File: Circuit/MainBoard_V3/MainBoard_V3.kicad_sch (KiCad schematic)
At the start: 0 parts

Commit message: 回路図と配置と配線が半分ほど終わり
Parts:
- added BZ1: Buzzer, Buzzer_Beeper:Buzzer_Murata_PKLCS1212E, symbol Device:Buzzer
- added C1, C12, C13, C14, C20, C21, C22, C23, C24, C26, C5: 0.1uf, Capacitor_SMD:C_0603_1608Metric, symbol Device:C
- added C10, C8: 100uf, Capacitor_THT:CP_Radial_D6.3mm_P2.50mm, symbol Device:C_Polarized
- added C11, C15, C17, C18, C19, C2, C27, C3, C4, C6, C7, C9: 10u, Capacitor_SMD:C_0805_2012Metric, symbol Device:C
- added C16: 4.7u, Capacitor_SMD:C_0805_2012Metric, symbol Device:C
- added C25: 2200pf, Capacitor_SMD:C_0603_1608Metric, symbol Device:C
- added D1, D2, D3, D7, D8: D_Schottky, Diode_SMD:D_SOD-323_HandSoldering, symbol Device:D_Schottky
- added D10, D11, D12, D13, D15, D16, D4, D5, D6, D9: LED, LED_SMD:LED_0603_1608Metric, symbol Device:LED
- added D14: CH213K, Package_TO_SOT_SMD:TSOT-23, symbol 0-MyLibrary:CH213K
- added F1, F2: Fuse, Fuse:Fuseholder_Clip-5x20mm_Keystone_3517_Inline_P23.11x6.76mm_D1.70mm_Horizontal, symbol Device:Fuse
- added H1, H2, H3, H4: MountingHole, MountingHole:MountingHole_3.2mm_M3_Pad_Via, symbol Mechanical:MountingHole
- added J1, J2, J3: Conn_01x02, Connector_JST:JST_PH_S2B-PH-K_1x02_P2.00mm_Horizontal, symbol Connector_Generic:Conn_01x02
- added J10, J11: Conn_01x03, Connector_JST:JST_PH_S3B-PH-K_1x03_P2.00mm_Horizontal, symbol Connector_Generic:Conn_01x03
- added J12, J13, J4: Conn_01x04, Connector_JST:JST_XH_S4B-XH-A-1_1x04_P2.50mm_Horizontal, symbol Connector_Generic:Conn_01x04
- added J14, J15: Conn_01x04, Connector_JST:JST_PH_S4B-PH-K_1x04_P2.00mm_Horizontal, symbol Connector_Generic:Conn_01x04
- added J5, J6, J7: Conn_01x02, Connector_Molex:Molex_SPOX_5268-02A_1x02_P2.50mm_Horizontal, symbol Connector_Generic:Conn_01x02
- added J8: Conn_01x07, Connector_JST:JST_PH_S7B-PH-K_1x07_P2.00mm_Horizontal, symbol Connector_Generic:Conn_01x07
- added J9: Raspberry_Pi_2_3, 0-MyLibrary:raspberreyPi, symbol Connector:Raspberry_Pi_2_3
- added MD1: OKL-T_6-W12N-C, 0-MyLibrary:MURATA_OKL-T-6-W12N-C_0, symbol OKL-T_6-W12N-C:OKL-T_6-W12N-C
- added NT1: NetTie_2, NetTie:NetTie-2_SMD_Pad0.5mm, symbol Device:NetTie_2
- added Q1, Q2: Q_PMOS_GDS, Package_TO_SOT_SMD:TO-252-2, symbol Device:Q_PMOS_GDS
- added Q10, Q3, Q5, Q6, Q7, Q8, Q9: BSS138, Package_TO_SOT_SMD:SOT-23, symbol Transistor_FET:BSS138
- added Q4: IRLML6402, Package_TO_SOT_SMD:SOT-23, symbol Transistor_FET:IRLML6402
- added R1, R13, R15, R17, R19, R2, R25, R26, R27, R30, R32, R34, R36, R37, R38, R4, R42, R5, R6, R7: 10k, Resistor_SMD:R_0603_1608Metric, symbol Device:R
- added R10, R12, R21, R29, R31, R33, R35, R41: 10, Resistor_SMD:R_0603_1608Metric, symbol Device:R
- added R11, R14, R16, R18, R20, R22, R23, R24, R28, R39, R40, R8: 1k, Resistor_SMD:R_0603_1608Metric, symbol Device:R
- added R9: 330, Resistor_SMD:R_0603_1608Metric, symbol Device:R
- added SW1, SW2, SW3: SW_Push, Button_Switch_SMD:SW_SPST_PTS810, symbol Switch:SW_Push
- added SW4, SW5: SW_Slide_DPDT, 0-MyLibrary:IS-2235, symbol Switch:SW_Slide_DPDT
- added TP1, TP2, TP3, TP4: TestPoint, TestPoint:TestPoint_THTPad_D4.0mm_Drill2.0mm, symbol Connector:TestPoint
- added TP5, TP6, TP7: TestPoint, TestPoint:TestPoint_THTPad_D1.0mm_Drill0.5mm, symbol Connector:TestPoint
- added U1: STM32F446RETx, Package_QFP:LQFP-64_10x10mm_P0.5mm, symbol MCU_ST_STM32F4:STM32F446RETx
- added U2: LM1117MP-3.3, Package_TO_SOT_SMD:SOT-223-3_TabPin2, symbol Regulator_Linear:LM1117MP-3.3
- added U3: MPU-6050, Package_DFN_QFN:QFN-24-1EP_4x4mm_P0.5mm_EP2.15x2.15mm, symbol Sensor_Motion:MPU-6050
- added Y1: CSTNE16M0V530000R0, Crystal:Resonator_SMD_Murata_CSTxExxV-3Pin_3.0x1.1mm, symbol CSTNE16M0V530000R0:CSTNE16M0V530000R0
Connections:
- new net: D4.2 (A), R11.1
- new net: Q4.1 (G), Q5.3 (D), R15.2
- new net: D10.2 (A), R23.1
- new net: Q8.1 (G), R33.2, R34.2
- new net: D12.2 (A), R25.1
- new net: Q2.1 (G), R5.2, SW5.1 (A), SW5.6 (C)
- new net: Q3.3 (D), SW5.2 (B), SW5.5 (B)
- new net: Q3.1 (G), R12.2, R13.2
- new net: D2.1 (K), F1.2, Q1.3 (S), R4.1
- new net: Q1.1 (G), R4.2, SW4.1 (A), SW4.6 (C)
- new net: Q7.1 (G), R31.2, R32.2
- new net: Q9.1 (G), R35.2, R36.2
- new net: Q5.1 (G), R21.1, R27.2
- new net: Q6.1 (G), R29.2, R30.2
- new net: C16.1, U1.30 (VCAP_1)
- new net: D13.2 (A), R26.1
- new net: D6.2 (A), R16.1
- new net: BZ1.2 (-), Q6.3 (D), R28.1
- new net: R10.1, R9.1
- new net: D15.2 (A), R39.1
- new net: D9.2 (A), R22.1
- new net: C18.1, D14.3 (VI), D8.2 (A), U2.2 (VO)
- new net: R8.1, R9.2
- new net: MD1.6 (TRIM), R8.2
- new net: D3.1 (K), F2.2, Q2.3 (S), R5.1
- new net: D5.2 (A), R14.1
- new net: D11.2 (A), R24.1
- new net: D16.2 (A), R40.1
- new net: C25.1, U3.20 (CPOUT)
- new net: R6.2, U1.60 (BOOT0)
- new net: Q10.1 (G), R41.2, R42.2
- new net: C26.1, U3.10 (REGOUT)
- new net: U1.5 (PH0), Y1.1
- new net: U1.6 (PH1), Y1.3
- new net: J9.1 (3V3), J9.17 (3V3)
- new net +3V3: C11.1, C14.2, C19.2, C20.2, C21.2, C22.2, C23.1, C24.2, D14.2 (VO), J10.2 (Pin_2), J11.2 (Pin_2), J12.2 (Pin_2), J13.2 (Pin_2), J8.2 (Pin_2), R1.2, R23.2, R37.1, R38.1, SW2.2, SW3.2, TP6.1, U1.1 (VBAT), U1.13 (VDDA), U1.19 (VDD), U1.32 (VDD), U1.48 (VDD), U1.64 (VDD), U3.13 (VDD), U3.8 (VLOGIC)
- new net +5V: C17.2, C27.1, C3.1, C4.1, C5.1, D1.2 (A), D7.1 (K), D8.1 (K), J14.4 (Pin_4), J15.4 (Pin_4), J9.2 (5V), J9.4 (5V), MD1.4 (VOUT), MD1.5 (SENSE), Q4.2 (S), R15.1, R24.2, TP5.1, U2.3 (VI)
- new net +BATT: F1.1, TP1.1
- new net +BATTP: F2.1, TP2.1
- new net ADC1: J10.3 (Pin_3), U1.24 (PC4)
- new net ADC2: J11.3 (Pin_3), U1.21 (PA5)
- new net ADC3: U1.20 (PA4)
- new net BRAKE_LED: J15.3 (Pin_3), Q8.3 (D)
- new net BRAKE_LED_SIG: R33.1, U1.26 (PB0)
- new net BTN1: R2.1, SW2.1, U1.3 (PC14)
- new net BTN2: R7.1, SW3.1, U1.2 (PC13)
- new net BUZZER: J9.12 (GPIO18/PWM0), R29.1, U1.55 (PB3)
- new net ECHO1: J12.3 (Pin_3), U1.50 (PA15)
- new net ECHO2: J13.3 (Pin_3), U1.41 (PA8)
- new net ECHO3: U1.40 (PC9)
- new net ECHO4: U1.36 (PB15)
- new net ECHO5: U1.34 (PB13)
- new net GND: C1.1, C11.2, C12.1, C14.1, C15.2, C16.2, C17.1, C18.2, C19.1, C2.1, C20.1, C21.1, C22.1, C23.2, C24.1, C25.2, C26.2, C27.2, C3.2, C4.2, C5.2, C6.2, C8.2, D10.1 (K), D11.1 (K), D12.1 (K), D14.1 (GND), D15.1 (K), D16.1 (K), D4.1 (K), D5.1 (K), D6.1 (K), D9.1 (K), J10.1 (Pin_1), J11.1 (Pin_1), J12.1 (Pin_1), J13.1 (Pin_1), J4.1 (Pin_1), J8.1 (Pin_1), J9.14 (GND), J9.20 (GND), J9.25 (GND), J9.30 (GND), J9.34 (GND), J9.39 (GND), J9.6 (GND), J9.9 (GND), MD1.1 (~{ON}/OFF_CONTROL), MD1.3 (1_GROUND), MD1.7 (2_GROUND), NT1.1, Q10.2 (S), Q5.2 (S), Q6.2 (S), Q7.2 (S), Q8.2 (S), Q9.2 (S), R10.2, R18.1, R2.2, R27.1, R30.1, R32.1, R34.1, R36.1, R42.1, R6.1, R7.2, SW1.1, SW4.2 (B), SW4.5 (B), TP3.1, TP7.1, U1.12 (VSSA), U1.18 (VSS), U1.31 (VSS), U1.47 (VSS), U1.63 (VSS), U2.1 (GND), U3.1 (CLKIN), U3.11 (FSYNC), U3.18 (GND), U3.9 (AD0), Y1.2
- new net GNDP: C10.2, C13.1, C7.1, C9.1, D13.1 (K), J5.1 (Pin_1), J6.1 (Pin_1), J7.1 (Pin_1), NT1.2, Q3.2 (S), R13.1, R20.1, TP4.1
- new net HEAD_LED: J14.3 (Pin_3), Q7.3 (D)
- new net HEAD_LED_SIG: R31.1, U1.27 (PB1)
- new net INT: U1.25 (PC5), U3.12 (INT)
- new net LIDAR_5V: C15.1, D7.2 (A), J4.2 (Pin_2), Q4.3 (D)
- new net LIDAR_5V_SIG: R21.2
- new net LIDAR_OUT: J4.3 (Pin_3), U1.44 (PA11)
- new net LW_LED: J14.2 (Pin_2), J15.2 (Pin_2), Q9.3 (D)
- new net LW_LED_SIG: R35.1, U1.23 (PA7)
- new net NRST: C1.2, J8.5 (Pin_5), R1.1, SW1.2, U1.7 (NRST)
- new net PC_RX: J8.7 (Pin_7), U1.42 (PA9)
- new net PC_TX: J8.6 (Pin_6), U1.43 (PA10)
- new net POWER_SIG: R12.1
- new net RAS_LED1: J9.35 (GPIO19/MISO1), R39.2
- new net RAS_LED2: J9.33 (PWM1/GPIO13), R40.2
- new net RAS_RX: J9.10 (GPIO15/RXD), U1.37 (PC6)
- new net RAS_TX: J9.8 (GPIO14/TXD), U1.38 (PC7)
- new net RW_LED: J14.1 (Pin_1), J15.1 (Pin_1), Q10.3 (D)
- new net RW_LED_SIG: R41.1, U1.22 (PA6)
- new net RX2: J1.2 (Pin_2), U1.17 (PA3)
- new net RX3: J4.4 (Pin_4), U1.52 (PC11)
- new net RX4: J2.2 (Pin_2), U1.15 (PA1)
- new net RX5: J3.2 (Pin_2), U1.54 (PD2)
- new net SCL: R38.2, U1.61 (PB8), U3.23 (SCL)
- new net SDA: R37.2, U1.62 (PB9), U3.24 (SDA)
- new net STM_LED1: R11.2, U1.56 (PB4)
- new net STM_LED2: R14.2, U1.57 (PB5)
- new net STM_LED3: R16.2, U1.58 (PB6)
- new net STM_LED4: R22.2, U1.59 (PB7)
- new net SWCLK: J8.4 (Pin_4), U1.49 (PA14)
- new net SWDIO: J8.3 (Pin_3), U1.46 (PA13)
- new net TRIG1: J12.4 (Pin_4), U1.51 (PC10)
- new net TRIG2: J13.4 (Pin_4), U1.45 (PA12)
- new net TRIG3: U1.39 (PC8)
- new net TRIG4: U1.35 (PB14)
- new net TRIG5: U1.33 (PB12)
- new net TX2: J1.1 (Pin_1), U1.16 (PA2)
- new net TX4: J2.1 (Pin_1), U1.14 (PA0)
- new net TX5: J3.1 (Pin_1), U1.53 (PC12)
- new net VCC: BZ1.1 (+), C2.2, C6.1, C8.1, D1.1 (K), D2.2 (A), MD1.2 (VIN), Q1.2 (D), R17.2, R25.2, R28.2
- new net VCCP: C10.1, C7.2, C9.2, D3.2 (A), J5.2 (Pin_2), J6.2 (Pin_2), J7.2 (Pin_2), Q2.2 (D), R19.2, R26.2
- new net VOLTAGE: C12.2, R17.1, R18.2, U1.11 (PC3)
- new net VOLTAGEP: C13.2, R19.1, R20.2, U1.10 (PC2)
- no-connect marks 0 -> 4
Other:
- note added: "Connectors"
- note added: "LED"
- note added: "MPU6050"
- note added: "Mounting hole"
- note added: "RasPi"
- note added: "STM32 F446RE"
- note added: "Supply"

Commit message: 大体設計終わり あとGNDビア
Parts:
- removed R28: 1k, Resistor_SMD:R_0603_1608Metric, symbol Device:R
- removed TP5, TP6, TP7: TestPoint, TestPoint:TestPoint_THTPad_D1.0mm_Drill0.5mm, symbol Connector:TestPoint
- added C29: 100uf, Capacitor_THT:CP_Radial_D6.3mm_P2.50mm, symbol Device:C_Polarized
- added C8: 10u, Capacitor_SMD:C_0805_2012Metric, symbol Device:C
- renumbered C8 to C28
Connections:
- net ADC3 is gone; now on net ENCODER_LEFT: U1.20 (PA4)
- net ECHO3 is gone; now on net ECHO2: U1.40 (PC9)
- net ECHO4 is gone; now on net POWER_SIG: U1.36 (PB15)
- net ECHO5 is gone; now on net BTN2: U1.34 (PB13)
- net TRIG3 is gone; now on net TRIG2: U1.39 (PC8)
- net TRIG4 is gone; now on net BTN1: U1.35 (PB14)
- net BTN1: no longer U1.3 (PC14)
- net BTN2: no longer U1.2 (PC13)
- net BUZZER: now also U1.29 (PB10); no longer U1.55 (PB3)
- net ECHO1: now also U1.45 (PA12); no longer U1.50 (PA15)
- net ECHO2: no longer U1.41 (PA8)
- net GND: now also C8.2; no longer C28.2
- net GNDP: now also C28.2, C29.2
- net HEAD_LED_SIG: now also U1.22 (PA6); no longer U1.27 (PB1)
- net LIDAR_5V_SIG: now also U1.24 (PC4)
- net LIDAR_OUT: now also U1.41 (PA8); no longer U1.44 (PA11)
- net PC_RX: now also U1.53 (PC12); no longer U1.42 (PA9)
- net PC_TX: now also U1.54 (PD2); no longer U1.43 (PA10)
- net RAS_RX: now also U1.42 (PA9); no longer U1.37 (PC6)
- net RAS_TX: now also U1.43 (PA10); no longer U1.38 (PC7)
- net RW_LED_SIG: now also U1.27 (PB1); no longer U1.22 (PA6)
- net RX2: now also J1.1 (Pin_1); no longer J1.2 (Pin_2)
- net RX3: now also J3.1 (Pin_1); no longer J4.4 (Pin_4)
- net RX4: now also J2.1 (Pin_1); no longer J2.2 (Pin_2)
- net TRIG1: now also U1.44 (PA11); no longer U1.51 (PC10)
- net TRIG2: no longer U1.45 (PA12)
- net TX2: now also J1.2 (Pin_2); no longer J1.1 (Pin_1)
- net TX4: now also J2.2 (Pin_2); no longer J2.1 (Pin_1)
- net VCC: now also C8.1; no longer C28.1
- net VCCP: now also C28.1, C29.1
- net VOLTAGE: now also U1.10 (PC2); no longer U1.11 (PC3)
- net VOLTAGEP: now also U1.11 (PC3); no longer U1.10 (PC2)
- net ADC1 renamed ENCODER_LEFT
- net ENCODER_LEFT: no longer U1.24 (PC4)
- net ADC2 renamed ENCODER_RIGHT
- net RX5 renamed TX3
- net TX3: now also U1.51 (PC10); no longer U1.54 (PD2)
- net TRIG5: no longer names the net of U1.33 (PB12)
- removed net TX5: J3.1 (Pin_1), U1.53 (PC12)
- new net RX6: J4.4 (Pin_4), U1.38 (PC7)
- new net TX6: U1.37 (PC6)
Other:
- moved on the sheet: C28, J11

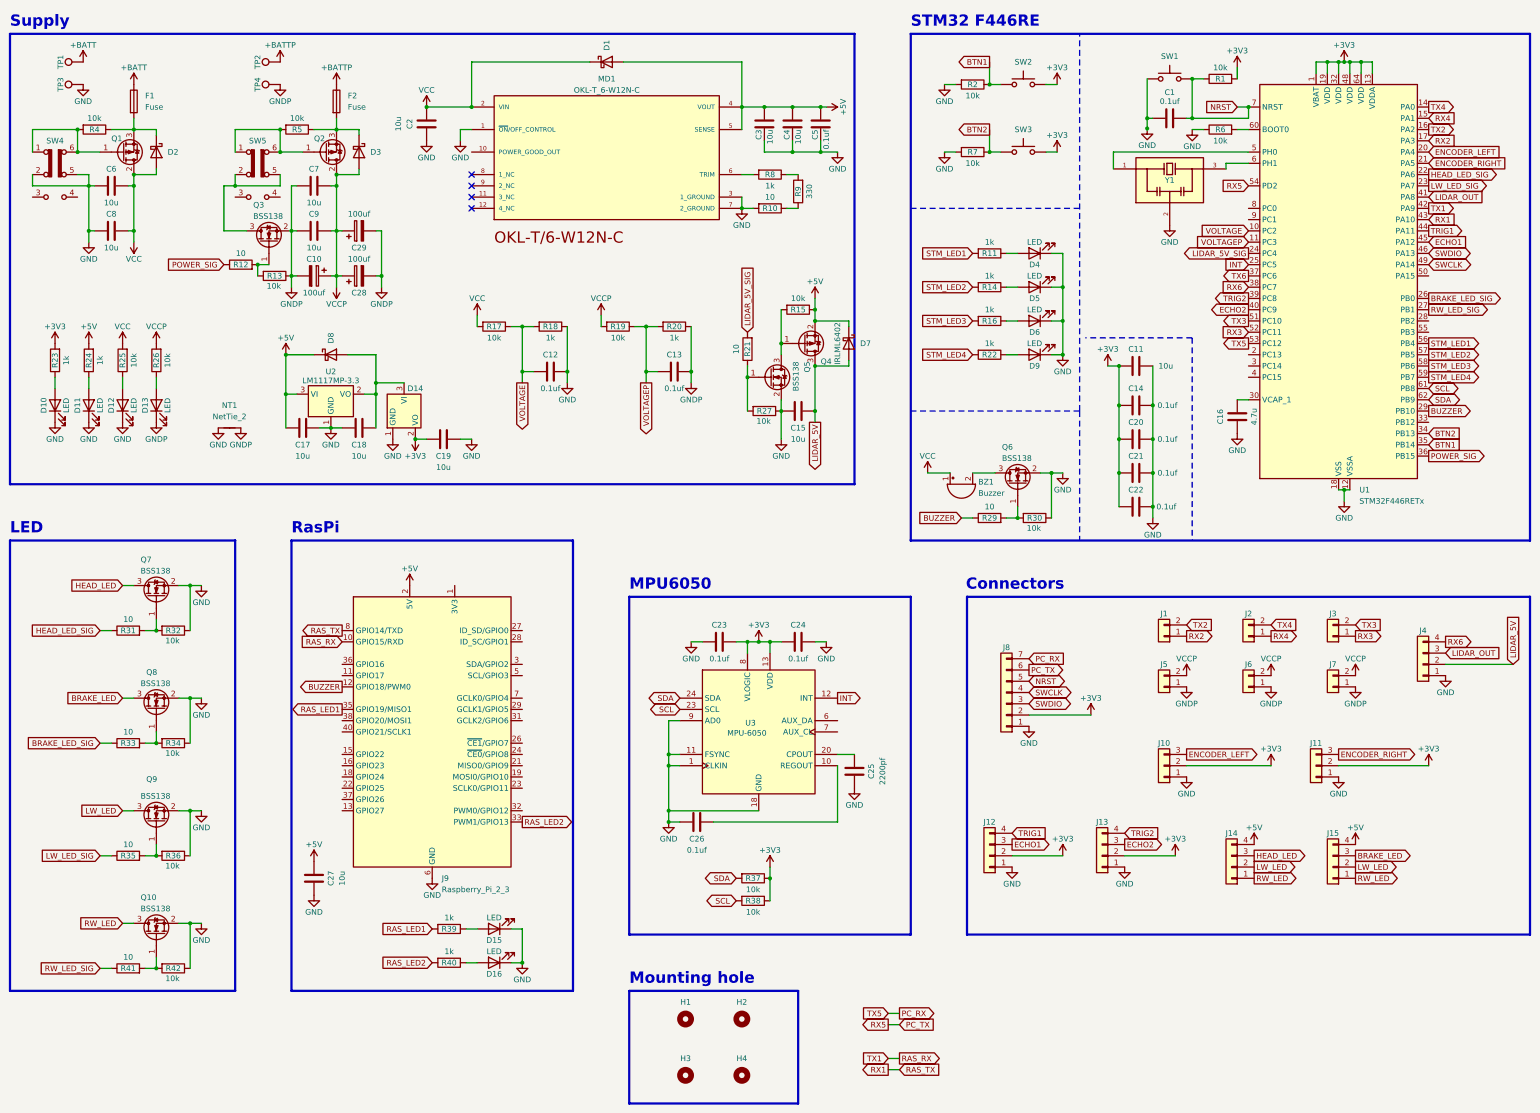
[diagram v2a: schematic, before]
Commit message: 電流センスの追加と設計大体終わり
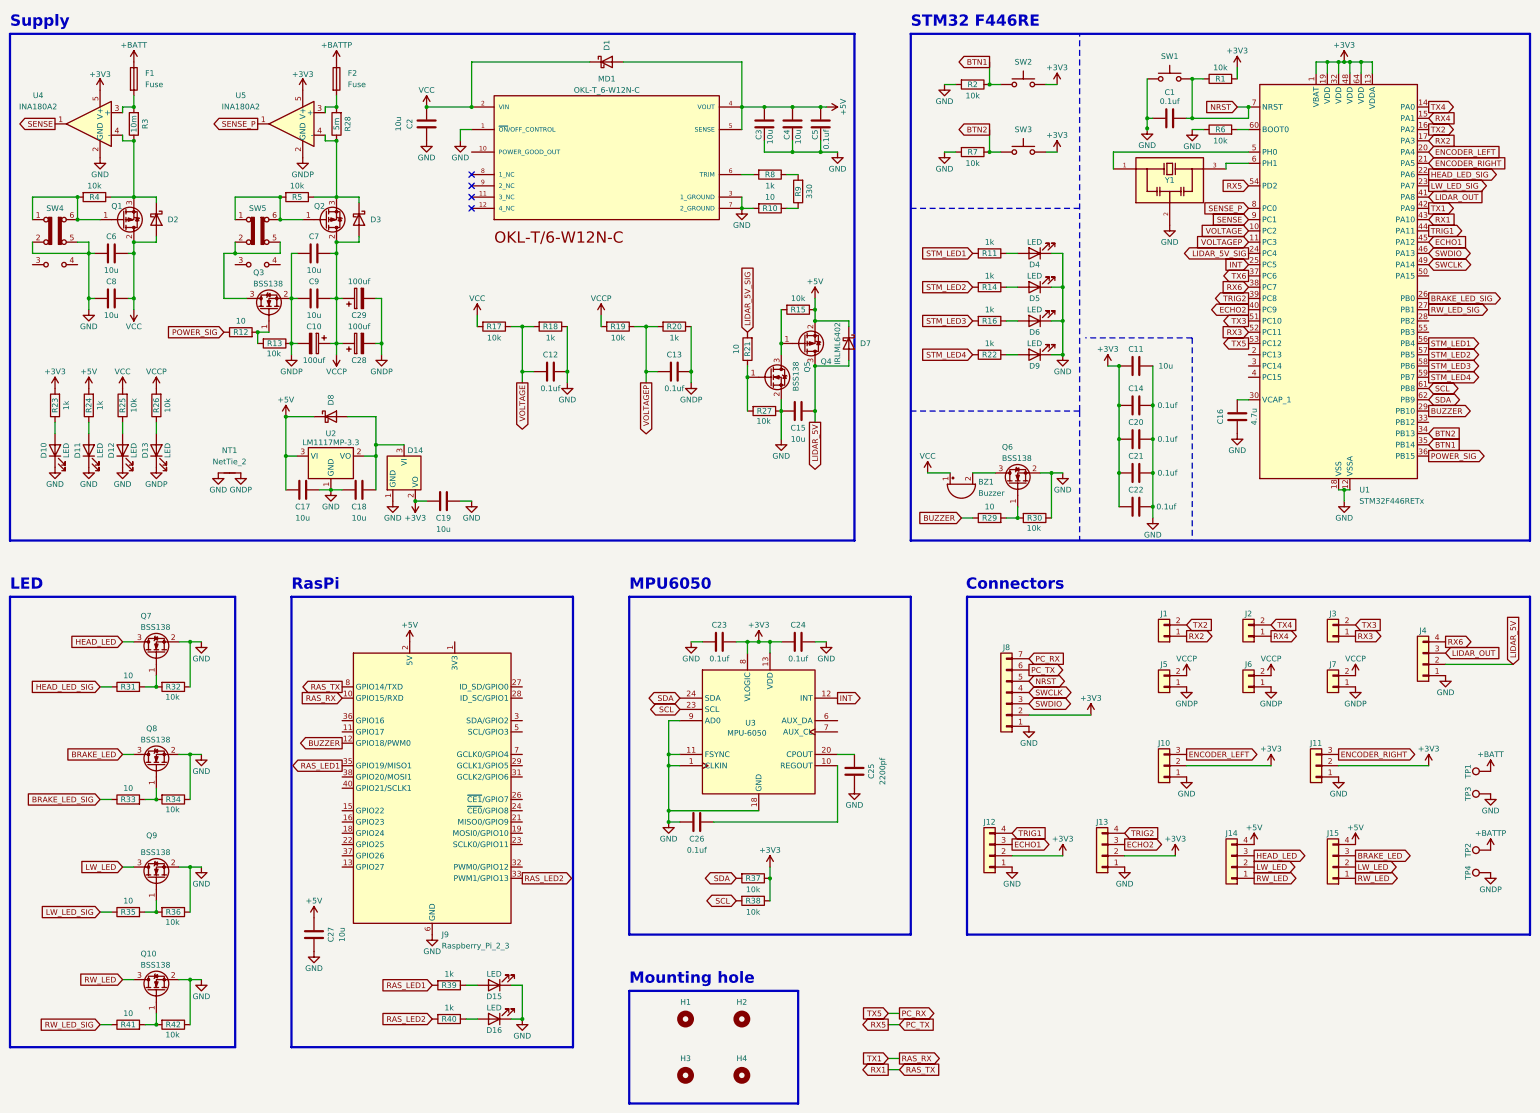
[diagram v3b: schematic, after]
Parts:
- added R28: 5m, Resistor_SMD:R_1206_3216Metric, symbol Device:R
- added R3: 10m, Resistor_SMD:R_1206_3216Metric, symbol Device:R
- added U4, U5: INA180A2, Package_TO_SOT_SMD:SOT-23-5, symbol Amplifier_Current:INA180A2
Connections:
- net +3V3: now also U4.5 (V+), U5.5 (V+)
- net GND: now also U4.2 (GND)
- net GNDP: now also U5.2 (GND)
- net at D2.1 (K), Q1.3 (S), R4.1: now also R3.1, U4.4 (-); no longer F1.2
- net at D3.1 (K), Q2.3 (S), R5.1: now also R28.1, U5.4 (-); no longer F2.2
- net SENSE_P: now reaches U1.8 (PC0)
- net SENSE_P: now also U5.1
- net SENSE: now reaches U1.9 (PC1)
- net SENSE: now also U4.1
- new net: F1.2, R3.2, U4.3 (+)
- new net: F2.2, R28.2, U5.3 (+)
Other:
- moved on the sheet: C10, C17, C18, C19, C27, C28, C29, C6, C7, C8, C9, D10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

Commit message: 完成&製造ファイル生成
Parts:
- added C30, C31, C32: 10u, Capacitor_SMD:C_0805_2012Metric, symbol Device:C
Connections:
- net +5V: now also C30.1, C31.1, C32.1
- net GND: now also C30.2, C31.2, C32.2
- net PGO: now reaches MD1.10 (POWER_GOOD_OUT)
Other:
- moved on the sheet: C11, C27, D15, D16, R39, R40

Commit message: 製造ファイル再生成
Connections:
- net PGO: no longer names the net of MD1.10 (POWER_GOOD_OUT)
- no-connect marks 4 -> 5
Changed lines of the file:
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@@
 	)
 	(junction
-		(at 281.94 46.7474)
-		(diameter 0)
-		(color 0 0 0 0)
-	)
-	(junction
 		(at 99.06 95.25)
 		(diameter 0)
@@
 	)
 	(no_connect
+		(at 129.54 52.07)
+	)
+	(no_connect
 		(at 129.54 57.15)
 	)
@@
 	(wire
 		(pts
-			(xy 281.94 46.99) (xy 281.94 46.7474)
-		)
-		(stroke
-			(width 0)
-			(type default)
-		)
-	)
-	(wire
-		(pts
 			(xy 148.59 240.03) (xy 148.59 247.65)
 		)
@@
 	(wire
 		(pts
-			(xy 281.94 46.7474) (xy 281.94 44.45)
-		)
-		(stroke
-			(width 0)
-			(type default)
-		)
-	)
-	(wire
-		(pts
 			(xy 104.14 62.23) (xy 99.06 62.23)
 		)
@@
 	(wire
 		(pts
+			(xy 281.94 44.45) (xy 281.94 46.99)
+		)
+		(stroke
+			(width 0)
+			(type default)
+		)
+	)
+	(wire
+		(pts
 			(xy 50.8 49.53) (xy 53.34 49.53)
 		)
@@
 		)
 	)
-	(global_label "PGO"
-		(shape output)
-		(at 129.54 52.07 180)
-		(fields_autoplaced yes)
-		(effects
-			(font
-				(size 1.27 1.27)
-			)
-			(justify right)
-		)
-		(property "Intersheetrefs" "${INTERSHEET_REFS}"
-			(at 122.6843 52.07 0)
-			(effects
-				(font
-					(size 1.27 1.27)
-				)
-				(justify right)
-				(hide yes)
-			)
-		)
-	)
 	(symbol
 		(lib_id "power:GND")
-		(at 281.94 46.7474 0)
+		(at 281.94 46.99 0)
 		(unit 1)
 		(exclude_from_sim no)
@@
 		(dnp no)
 		(property "Reference" "#PWR013"
-			(at 281.94 53.0974 0)
+			(at 281.94 53.34 0)
 			(effects
 				(font
@@
 		)
 		(property "Value" "GND"
-			(at 281.94 50.5574 0)
+			(at 281.94 50.8 0)
 			(effects
 				(font
@@
 		)
 		(property "Footprint" ""
-			(at 281.94 46.7474 0)
+			(at 281.94 46.99 0)
 			(effects
 				(font
@@
 		)
 		(property "Datasheet" ""
-			(at 281.94 46.7474 0)
+			(at 281.94 46.99 0)
 			(effects
 				(font
@@
 		)
 		(property "Description" "Power symbol creates a global label with name \"GND\" , ground"
-			(at 281.94 46.7474 0)
+			(at 281.94 46.99 0)
 			(effects
 				(font
